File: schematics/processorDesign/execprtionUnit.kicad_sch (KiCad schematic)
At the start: 25 parts

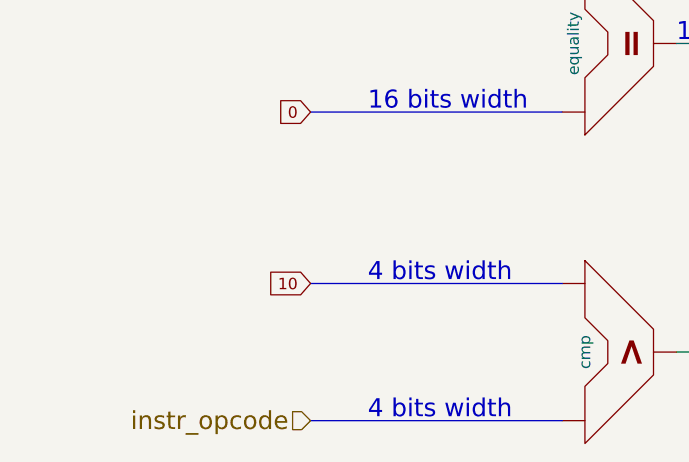
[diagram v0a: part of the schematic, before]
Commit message: the interrupt is now working correctly
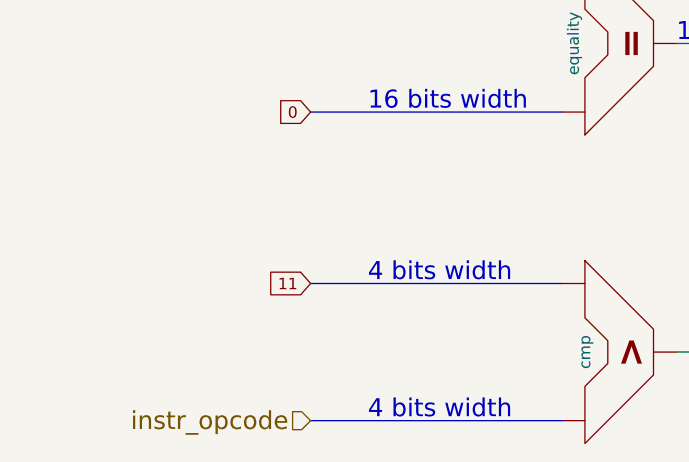
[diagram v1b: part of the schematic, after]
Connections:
- net at U?.: now also U?.1
- new net: U?., U?. (select), U?.1
- new net: U?., U?. (select), U?.2
- now unconnected: U?., U?., U?. (select), U?. (select)
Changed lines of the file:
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@@
     )
   )
-  (global_label "10" (shape input) (at 46.99 261.62 180) (fields_autoplaced)
+  (global_label "11" (shape input) (at 46.99 261.62 180) (fields_autoplaced)
     (effects (font (size 1.27 1.27)) (justify right))
     (property "Intersheet References" "${INTERSHEET_REFS}" (id 0) (at 42.1579 261.5406 0)

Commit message: the processor is now up and running , tested and verified , except for the part related to labels due to a bug in the assembler
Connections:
- net at U?.: now also U?.1
- new net: U?., U?. (select), U?.1
- new net: U?., U?. (select), U?.2
- now unconnected: U?., U?., U?. (select), U?. (select)

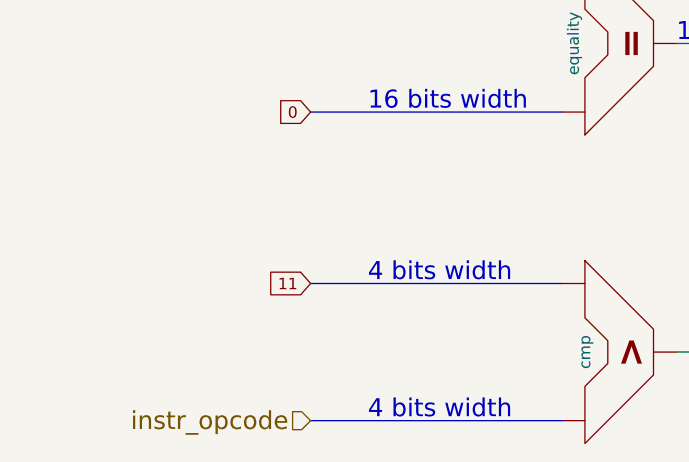
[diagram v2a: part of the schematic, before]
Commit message: the processor is now up and running , tested and verified completly for almost most of the things
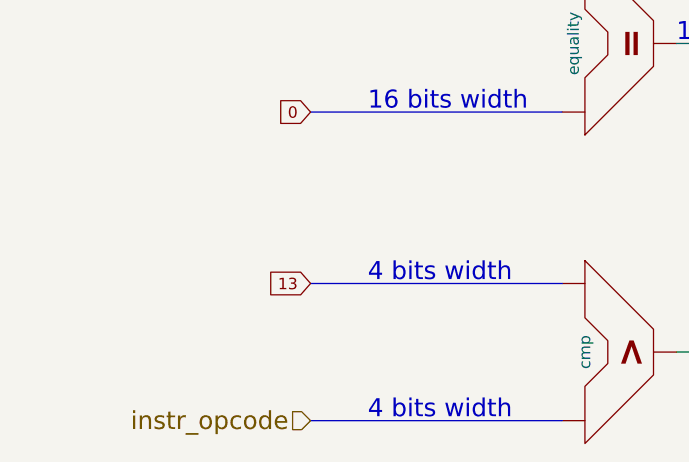
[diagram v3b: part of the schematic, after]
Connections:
- net at U?.: now also U?.1
- new net: U?., U?. (select), U?.1
- new net: U?., U?. (select), U?.2
- now unconnected: U?., U?., U?. (select), U?. (select)
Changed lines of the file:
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@@
     )
   )
-  (global_label "11" (shape input) (at 46.99 261.62 180) (fields_autoplaced)
+  (global_label "13" (shape input) (at 46.99 261.62 180) (fields_autoplaced)
     (effects (font (size 1.27 1.27)) (justify right))
     (property "Intersheet References" "${INTERSHEET_REFS}" (id 0) (at 42.1579 261.5406 0)

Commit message: added small code to EDU
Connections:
- net at U?.: now also U?.1
- new net: U?., U?. (select), U?.1
- new net: U?., U?. (select), U?.2
- now unconnected: U?., U?., U?. (select), U?. (select)
